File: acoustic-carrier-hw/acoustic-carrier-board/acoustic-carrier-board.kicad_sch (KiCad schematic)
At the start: 0 parts

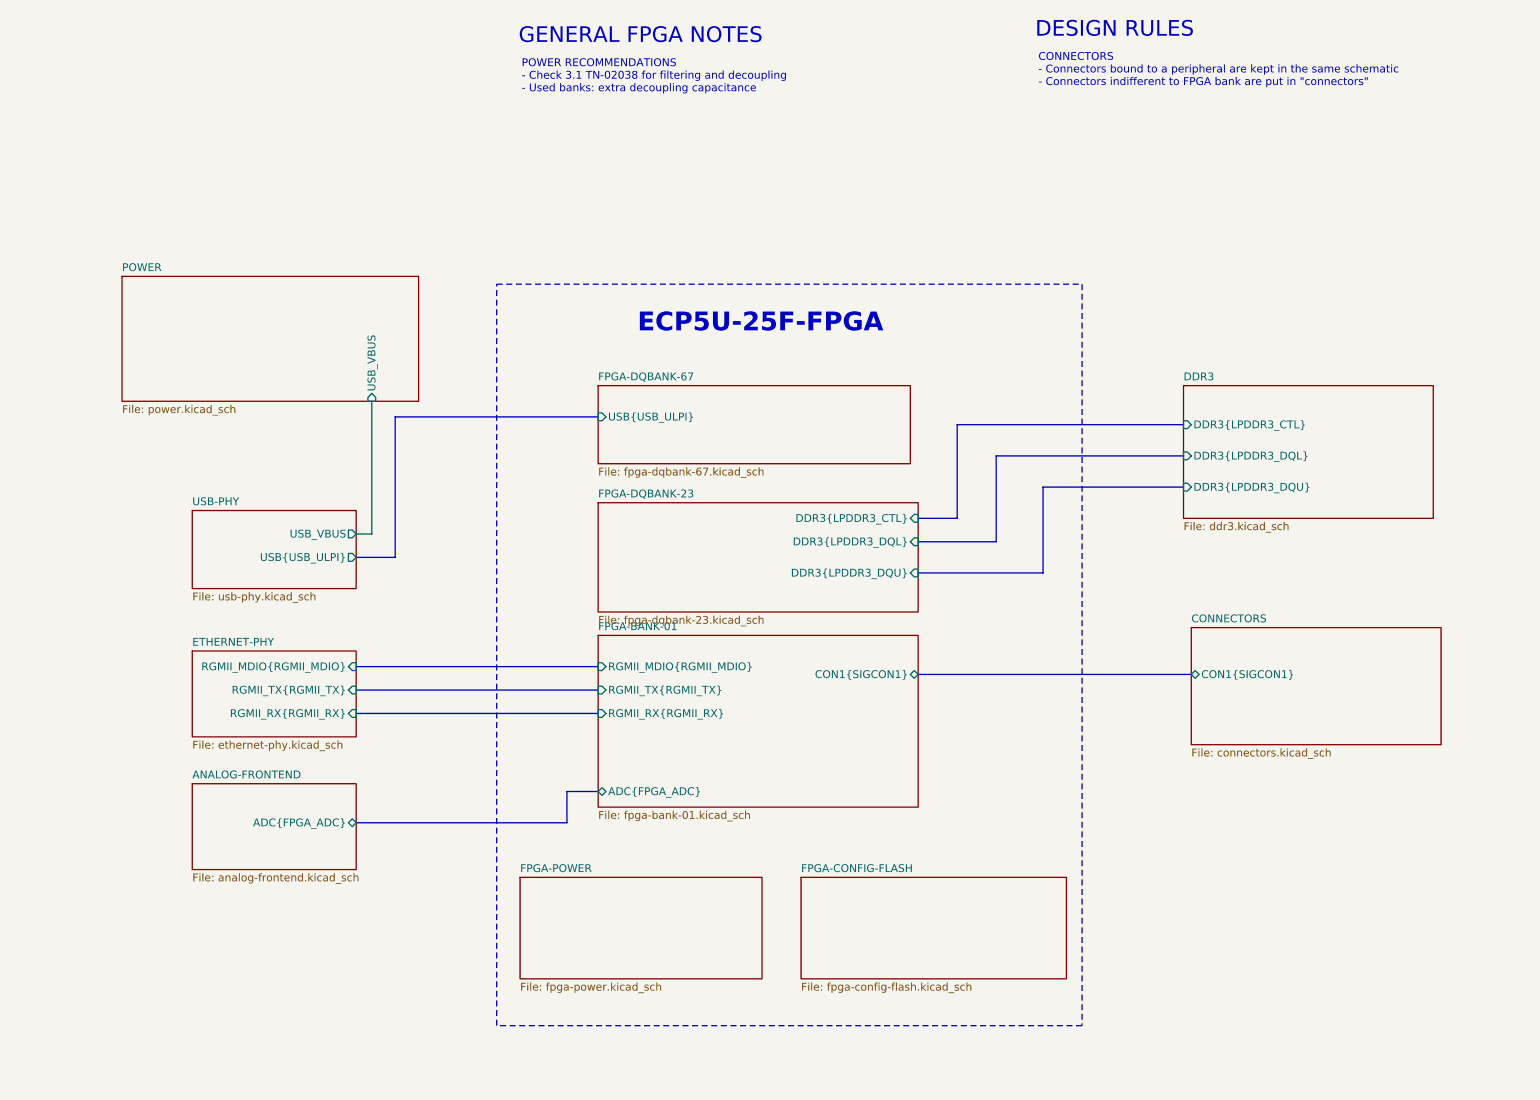
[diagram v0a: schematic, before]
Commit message: [carrier] connected ethernet, usb and adc to appropriate banks, redpositioned schmitt trigger and USB
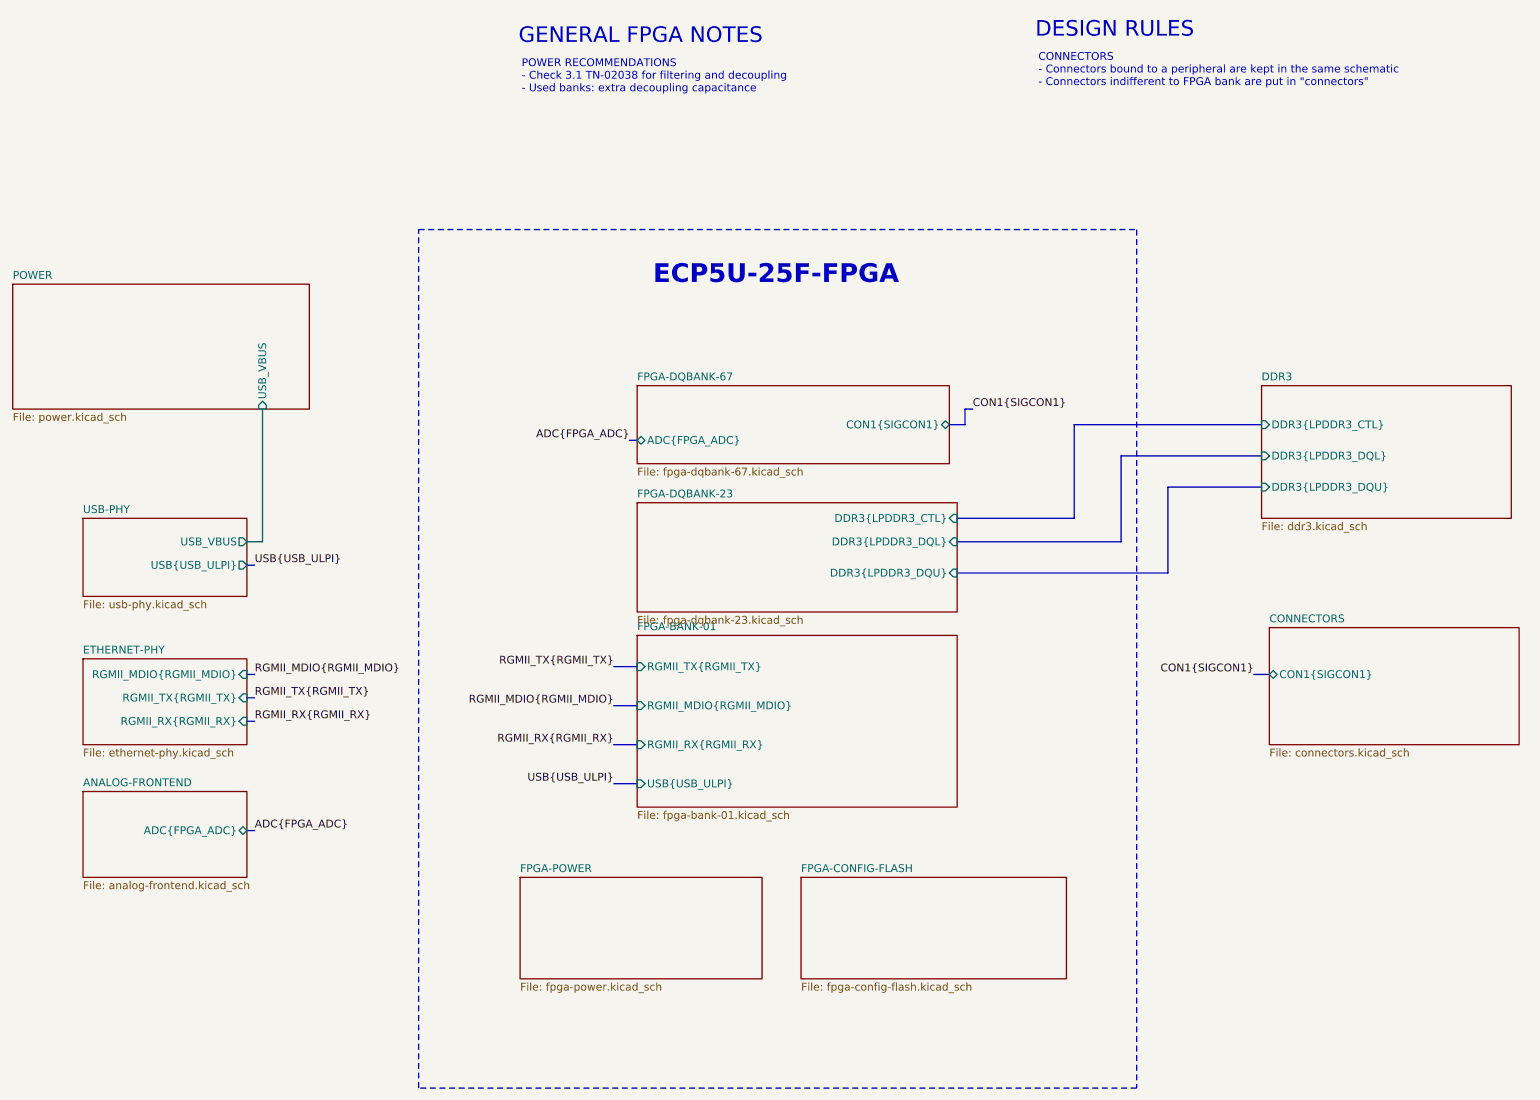
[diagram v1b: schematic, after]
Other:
- sheet FPGA-BANK-01 ports: added USB{USB_ULPI}; removed ADC{FPGA_ADC}, CON1{SIGCON1}
- sheet FPGA-DQBANK-67 ports: added ADC{FPGA_ADC}, CON1{SIGCON1}; removed USB{USB_ULPI}

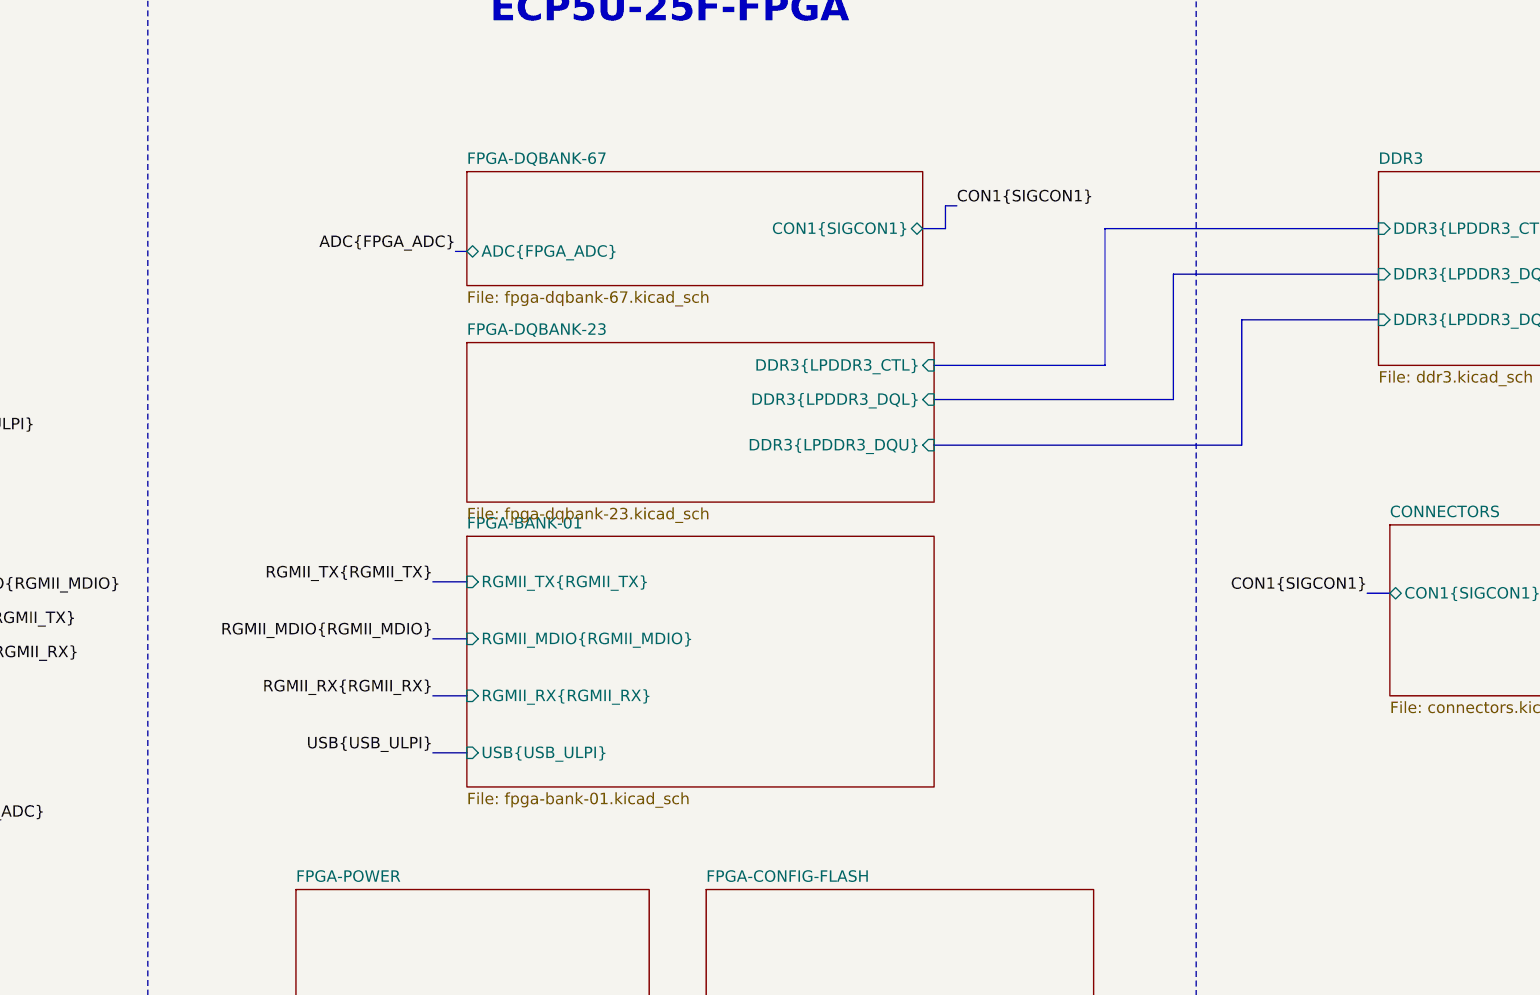
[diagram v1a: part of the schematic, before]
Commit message: [¢arrier] Placed power supply circuitry appropraitely, changed power connector (next) Place schmitt triggers between usb and power, put critical circuitry closer together, place config circuitry
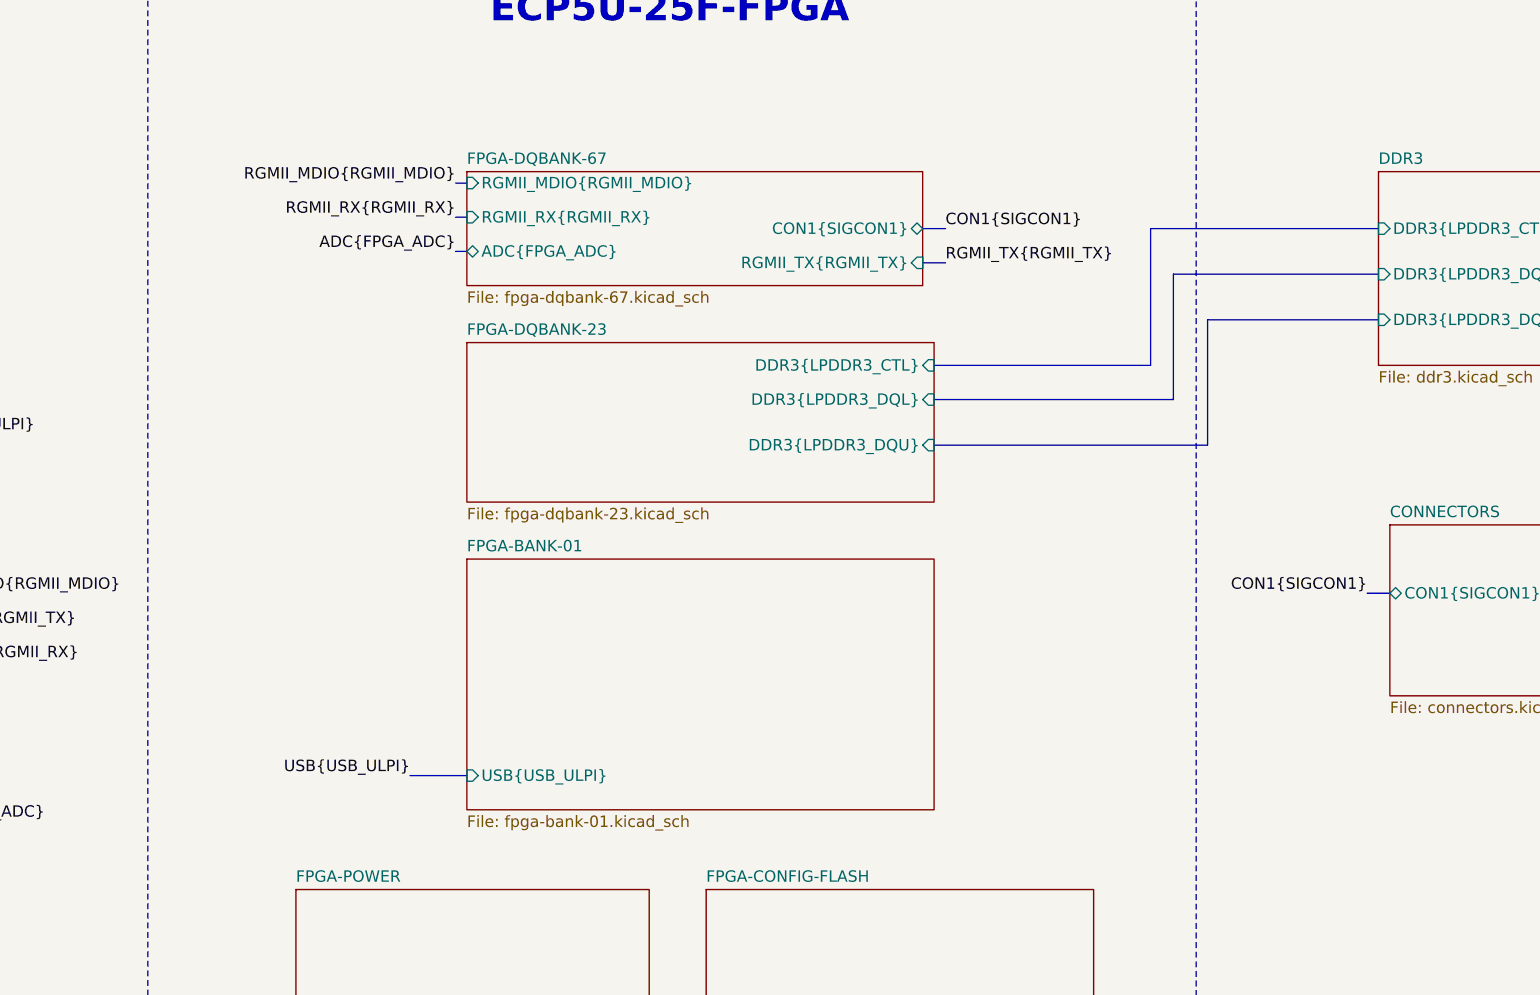
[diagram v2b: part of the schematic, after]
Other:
- sheet FPGA-BANK-01 ports: added none; removed RGMII_MDIO{RGMII_MDIO}, RGMII_RX{RGMII_RX}, RGMII_TX{RGMII_TX}
- sheet FPGA-DQBANK-67 ports: added RGMII_MDIO{RGMII_MDIO}, RGMII_RX{RGMII_RX}, RGMII_TX{RGMII_TX}; removed none
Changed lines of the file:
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@@
 	(bus
 		(pts
-			(xy 194.31 52.07) (xy 224.79 52.07)
+			(xy 199.39 52.07) (xy 224.79 52.07)
 		)
 		(stroke
@@
 	(bus
 		(pts
-			(xy 209.55 62.23) (xy 224.79 62.23)
+			(xy 205.74 62.23) (xy 224.79 62.23)
 		)
 		(stroke
@@
 		)
 	)
-	(bus
-		(pts
-			(xy 176.53 52.07) (xy 176.53 49.53)
-		)
-		(stroke
-			(width 0)
-			(type default)
-		)
-	)
 	(wire
 		(pts
@@
 	(bus
 		(pts
-			(xy 119.38 110.49) (xy 123.19 110.49)
+			(xy 116.84 113.03) (xy 123.19 113.03)
 		)
 		(stroke
@@
 	(bus
 		(pts
-			(xy 123.19 91.44) (xy 119.38 91.44)
-		)
-		(stroke
-			(width 0)
-			(type default)
-		)
-	)
-	(bus
-		(pts
 			(xy 59.69 92.71) (xy 60.96 92.71)
 		)
@@
 	(bus
 		(pts
-			(xy 209.55 76.2) (xy 175.26 76.2)
+			(xy 205.74 76.2) (xy 175.26 76.2)
 		)
 		(stroke
@@
 	(bus
 		(pts
-			(xy 175.26 67.31) (xy 194.31 67.31)
-		)
-		(stroke
-			(width 0)
-			(type default)
-		)
-	)
-	(bus
-		(pts
-			(xy 123.19 97.79) (xy 119.38 97.79)
-		)
-		(stroke
-			(width 0)
-			(type default)
-		)
-	)
-	(bus
-		(pts
-			(xy 123.19 104.14) (xy 119.38 104.14)
+			(xy 175.26 67.31) (xy 199.39 67.31)
 		)
 		(stroke
@@
 	(bus
 		(pts
-			(xy 176.53 49.53) (xy 177.8 49.53)
-		)
-		(stroke
-			(width 0)
-			(type default)
-		)
-	)
-	(bus
-		(pts
-			(xy 209.55 62.23) (xy 209.55 76.2)
-		)
-		(stroke
-			(width 0)
-			(type default)
-		)
-	)
-	(bus
-		(pts
-			(xy 194.31 67.31) (xy 194.31 52.07)
+			(xy 123.19 50.8) (xy 121.92 50.8)
+		)
+		(stroke
+			(width 0)
+			(type default)
+		)
+	)
+	(bus
+		(pts
+			(xy 205.74 62.23) (xy 205.74 76.2)
+		)
+		(stroke
+			(width 0)
+			(type default)
+		)
+	)
+	(bus
+		(pts
+			(xy 199.39 67.31) (xy 199.39 52.07)
+		)
+		(stroke
+			(width 0)
+			(type default)
+		)
+	)
+	(bus
+		(pts
+			(xy 173.99 55.88) (xy 176.53 55.88)
+		)
+		(stroke
+			(width 0)
+			(type default)
+		)
+	)
+	(bus
+		(pts
+			(xy 123.19 46.99) (xy 121.92 46.99)
 		)
 		(stroke
@@
 		)
 	)
-	(label "RGMII_MDIO{RGMII_MDIO}"
-		(at 119.38 97.79 180)
+	(label "RGMII_RX{RGMII_RX}"
+		(at 121.92 50.8 180)
 		(effects
 			(font
@@
 	)
 	(label "CON1{SIGCON1}"
-		(at 177.8 49.53 0)
+		(at 176.53 52.07 0)
 		(effects
 			(font
@@
 		)
 	)
-	(label "RGMII_TX{RGMII_TX}"
-		(at 119.38 91.44 180)
-		(effects
-			(font
-				(size 1.27 1.27)
-			)
-			(justify right bottom)
-		)
-	)
 	(label "USB{USB_ULPI}"
-		(at 119.38 110.49 180)
+		(at 116.84 113.03 180)
 		(effects
 			(font
@@
 	)
 	(label "RGMII_RX{RGMII_RX}"
-		(at 119.38 104.14 180)
+		(at 60.96 100.33 0)
+		(effects
+			(font
+				(size 1.27 1.27)
+			)
+			(justify left bottom)
+		)
+	)
+	(label "RGMII_TX{RGMII_TX}"
+		(at 176.53 55.88 0)
+		(effects
+			(font
+				(size 1.27 1.27)
+			)
+			(justify left bottom)
+		)
+	)
+	(label "RGMII_MDIO{RGMII_MDIO}"
+		(at 121.92 46.99 180)
 		(effects
 			(font
@@
 			)
 			(justify right bottom)
-		)
-	)
-	(label "RGMII_RX{RGMII_RX}"
-		(at 60.96 100.33 0)
-		(effects
-			(font
-				(size 1.27 1.27)
-			)
-			(justify left bottom)
 		)
 	)
@@
 	)
 	(sheet
-		(at 123.19 86.36)
+		(at 123.19 88.9)
 		(size 52.07 27.94)
 		(exclude_from_sim no)
@@
 		)
 		(property "Sheetname" "FPGA-BANK-01"
-			(at 123.19 85.6484 0)
+			(at 123.19 88.1884 0)
 			(effects
 				(font
@@
 		)
 		(property "Sheetfile" "fpga-bank-01.kicad_sch"
-			(at 123.19 114.8846 0)
+			(at 123.19 117.4246 0)
 			(effects
 				(font
@@
 			)
 		)
-		(pin "RGMII_TX{RGMII_TX}" input
-			(at 123.19 91.44 180)
-			(effects
-				(font
-					(size 1.27 1.27)
-				)
-				(justify left)
-			)
-		)
-		(pin "RGMII_MDIO{RGMII_MDIO}" input
-			(at 123.19 97.79 180)
-			(effects
-				(font
-					(size 1.27 1.27)
-				)
-				(justify left)
-			)
-		)
-		(pin "RGMII_RX{RGMII_RX}" input
-			(at 123.19 104.14 180)
-			(effects
-				(font
-					(size 1.27 1.27)
-				)
-				(justify left)
-			)
-		)
 		(pin "USB{USB_ULPI}" input
-			(at 123.19 110.49 180)
+			(at 123.19 113.03 180)
 			(effects
 				(font
@@
 			(effects
 				(font
+					(size 1.27 1.27)
+				)
+				(justify right)
+			)
+		)
+		(pin "RGMII_RX{RGMII_RX}" input
+			(at 123.19 50.8 180)
+			(effects
+				(font
+					(size 1.27 1.27)
+				)
+				(justify left)
+			)
+		)
+		(pin "RGMII_MDIO{RGMII_MDIO}" input
+			(at 123.19 46.99 180)
+			(effects
+				(font
+					(size 1.27 1.27)
+				)
+				(justify left)
+			)
+		)
+		(pin "RGMII_TX{RGMII_TX}" input
+			(at 173.99 55.88 0)
+			(effects
+				(font
